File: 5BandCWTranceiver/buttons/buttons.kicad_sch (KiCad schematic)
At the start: 8 parts, among them J1 Conn_01x04_Female, SW1 SW_Push, SW2 SW_Push, SW3 SW_Push

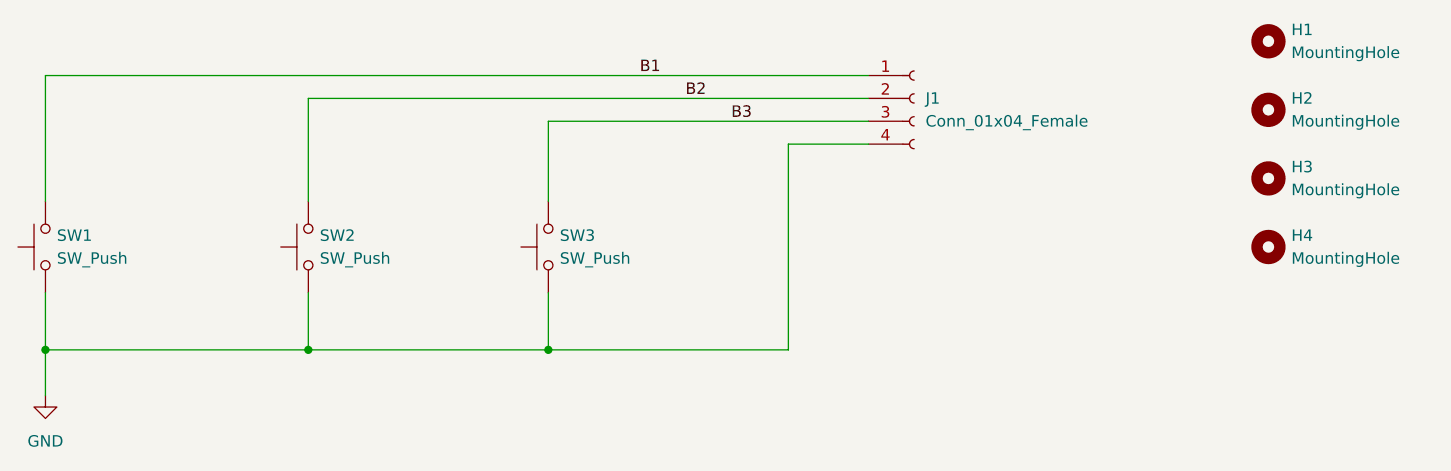
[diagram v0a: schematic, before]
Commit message: Board Tape Out
Final tapeout changes; board ordered
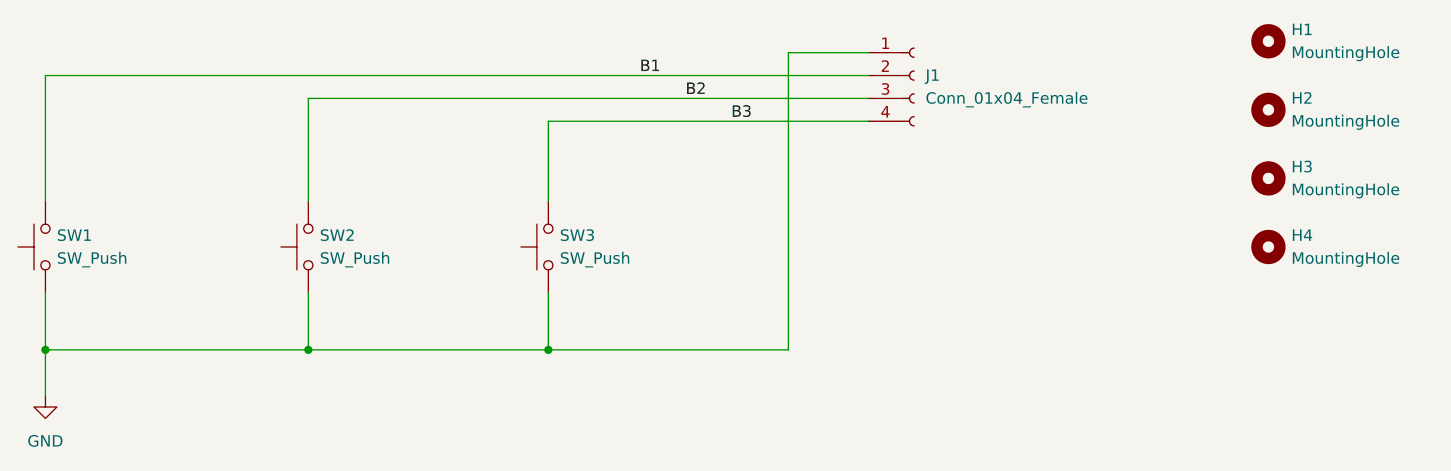
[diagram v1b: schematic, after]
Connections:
- net B1: now also J1.2 (Pin_2); no longer J1.1 (Pin_1)
- net B2: now also J1.3 (Pin_3); no longer J1.2 (Pin_2)
- net B3: now also J1.4 (Pin_4); no longer J1.3 (Pin_3)
- net GND: now also J1.1 (Pin_1); no longer J1.4 (Pin_4)
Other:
- moved on the sheet: J1
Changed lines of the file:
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@@
     (stroke (width 0) (type default) (color 0 0 0 0))
   )
-  (wire (pts (xy 152.4 83.82) (xy 143.51 83.82))
+  (wire (pts (xy 152.4 73.66) (xy 143.51 73.66))
     (stroke (width 0) (type default) (color 0 0 0 0))
   )
@@
     (stroke (width 0) (type default) (color 0 0 0 0))
   )
-  (wire (pts (xy 143.51 83.82) (xy 143.51 106.68))
+  (wire (pts (xy 143.51 73.66) (xy 143.51 106.68))
     (stroke (width 0) (type default) (color 0 0 0 0))
   )
@@
     (pin "2")
   )
-  (symbol (lib_id "Connector:Conn_01x04_Female") (at 157.48 78.74 0) (unit 1)
+  (symbol (lib_id "Connector:Conn_01x04_Female") (at 157.48 76.2 0) (unit 1)
     (in_bom yes) (on_board yes) (fields_autoplaced)
-    (property "Reference" "J1" (id 0) (at 158.75 78.7399 0)
+    (property "Reference" "J1" (id 0) (at 158.75 76.1999 0)
       (effects (font (size 1.27 1.27)) (justify left))
     )
-    (property "Value" "Conn_01x04_Female" (id 1) (at 158.75 81.2799 0)
+    (property "Value" "Conn_01x04_Female" (id 1) (at 158.75 78.7399 0)
       (effects (font (size 1.27 1.27)) (justify left))
     )
-    (property "Footprint" "Connector_PinHeader_2.54mm:PinHeader_1x04_P2.54mm_Vertical" (id 2) (at 157.48 78.74 0)
+    (property "Footprint" "Connector_PinHeader_2.54mm:PinHeader_1x04_P2.54mm_Vertical" (id 2) (at 157.48 76.2 0)
       (effects (font (size 1.27 1.27)) hide)
     )
-    (property "Datasheet" "~" (id 3) (at 157.48 78.74 0)
+    (property "Datasheet" "~" (id 3) (at 157.48 76.2 0)
       (effects (font (size 1.27 1.27)) hide)
     )
